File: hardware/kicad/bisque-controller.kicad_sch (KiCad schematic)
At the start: 49 parts, among them J1 USB-C, J2 5V_IN, J3 TC_K, J4 SSR, J5 DISPLAY, J6 NAV_SW, J7 AUX, Q1 AO3400A, Q2 AO3400A, SW1 RESET, SW2 BOOT, U1 ESP32-S3-WROOM-1-N16R8, U2 AMS1117-3.3, U3 MAX31855KASA+, U4 USBLC6-2SC6

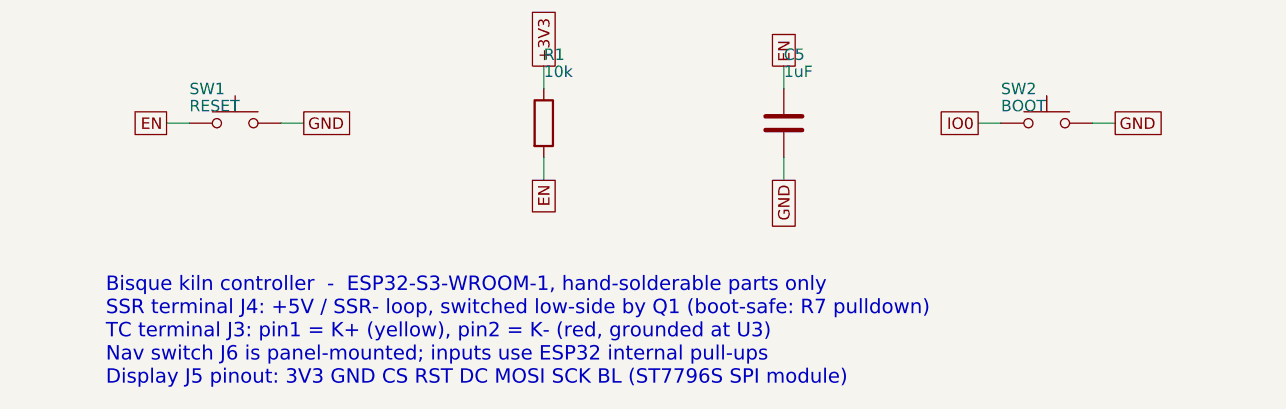
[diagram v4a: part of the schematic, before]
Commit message: hardware: target JLCPCB assembly, fix CPL rotations, refresh fab outputs
Drops the hand-solderable design constraint and makes the board orderable as
an assembled PCBA. Three BOM/CPL defects would have mis-assembled or skipped
parts, and the fab package had drifted from the board file.

gen_jlc.py:
- Apply JLCPCB's per-package rotation corrections when writing the CPL, and
  print each one so a regeneration is auditable. Previously the raw KiCad
  angle went straight through and rotation checking was deferred to JLC's
  order preview, which does not reliably catch 180-degree errors on polarized
  parts. Corrects U2 (SOT-223), Q1/Q2 (SOT-23), U4 (SOT-23-6) and U3
  (SOIC-8). Offsets come from the community table in
  bennymeg/Fabrication-Toolkit, which is derived from real JLCPCB order
  feedback; families absent from it (chip passives, SMA/SOD-123 diodes,
  PLCC-4, USB-C, terminal blocks, 2.54mm headers, tact switches) need no
  correction, so applying a blanket offset to the diodes would have reversed
  D1/D2.
- C9 was LCSC C57112, an imperial 0603 part sitting on an 0805 land pattern.
  Now C1710 (CL21B103KBANNNC, 10nF 50V X7R 0805, Basic).
- BZ1, J5, J6, J7, SW1 and SW2 had blank LCSC numbers, so JLC would not have
  populated them. All six now carry verified in-stock parts. A2547WV-8P was
  rejected for J5/J7 (zero stock) in favour of the genuine Molex 22-27-2081.
- Every entry re-verified against the LCSC catalog for package, value and
  stock; the CONFIRM-at-order-time markers are gone.
- Flag through-hole lines in the BOM (detected from the footprint attr): the
  nine THT parts need JLC's Standard assembly, and its through-hole coverage
  is narrower than its SMD coverage.

Fab outputs: re-exported gerbers, drill, drill map and job file. These were
generated before the board's final zone refill, so F_Cu carried a stale GND
pour outline near the USB-C connector (three vertices collapsing to two,
~80um). Everything else was already geometry-identical. The READM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
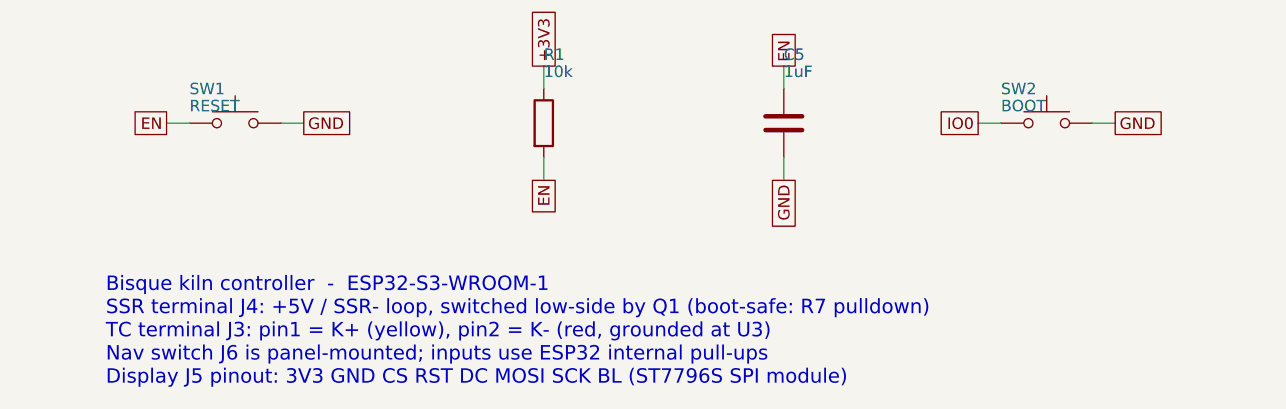
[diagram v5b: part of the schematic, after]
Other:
- note added: "Bisque kiln controller - ESP32-S3-WROOM-1 SSR terminal J4: +5V / SSR- loop, switched low-side by Q1 (boot-safe: R7 pulldown) TC terminal J3: pin1 = K+ (yellow), pin2 = K- (red, grounded at U3) Nav switch J6 is panel-mounted; inputs use ESP32 internal pull-ups Display J5 pinout: 3V3 GND CS RST DC MOSI SCK BL (ST7796S SPI module)"
- note removed: "Bisque kiln controller - ESP32-S3-WROOM-1, hand-solderable parts only SSR terminal J4: +5V / SSR- loop, switched low-side by Q1 (boot-safe: R7 pulldown) TC terminal J3: pin1 = K+ (yellow), pin2 = K- (red, grounded at U3) Nav switch J6 is panel-mounted; inputs use ESP32 internal pull-ups Display J5 pinout: 3V3 GND CS RST DC MOSI SCK BL (ST7796S SPI module)"
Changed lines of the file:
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@@
 		(company "Bisque project")
 		(comment 1 "ESP32-S3-WROOM-1 + MAX31855 + SSR drive")
-		(comment 2 "Hand-solderable: >=0805, SOIC, SOT, THT connectors")
+		(comment 2 "2-layer, 100 x 80 mm, JLCPCB standard process")
 	)
 	(symbol (lib_id "RF_Module:ESP32-S3-WROOM-1") (at 170.18 165.1 0) (unit 1)
@@
 		(effects (font (size 2 2) bold) (justify left))
 	)
-	(text "Bisque kiln controller  -  ESP32-S3-WROOM-1, hand-solderable parts only\nSSR terminal J4: +5V / SSR- loop, switched low-side by Q1 (boot-safe: R7 pulldown)\nTC terminal J3: pin1 = K+ (yellow), pin2 = K- (red, grounded at U3)\nNav switch J6 is panel-mounted; inputs use ESP32 internal pull-ups\nDisplay J5 pinout: 3V3 GND CS RST DC MOSI SCK BL (ST7796S SPI module)" (at 25 281 0)
+	(text "Bisque kiln controller  -  ESP32-S3-WROOM-1\nSSR terminal J4: +5V / SSR- loop, switched low-side by Q1 (boot-safe: R7 pulldown)\nTC terminal J3: pin1 = K+ (yellow), pin2 = K- (red, grounded at U3)\nNav switch J6 is panel-mounted; inputs use ESP32 internal pull-ups\nDisplay J5 pinout: 3V3 GND CS RST DC MOSI SCK BL (ST7796S SPI module)" (at 25 281 0)
 		(effects (font (size 1.6 1.6)) (justify left))
 	)

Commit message: hardware: move display to +5V power, correct 3.5"->4.0" everywhere
Switches the KiCad PCB's display header (J5) from +3V3 to +5V power, per
the user's own hardware: a 4.0" LCDWIKI ST7796S module (MSP4020/MSP4021),
not the 3.5" panel this project previously assumed.

design.py: J5 pin 1 and its local decoupling cap C12 move from +3V3 to
+5V. Verified pin-compatible against the module's own manual (LCDWiki's
product page returned only marketing copy; the linked PDF is a 24-page
scan with no embedded fonts, so it had to be rendered and read directly) -
pins 1-8 are VCC/GND/CS/RESET/DC/SDI/SCK/LED, an exact match for J5's
existing assignment, and VCC is rated 3.3-5V with every reference wiring
diagram in the manual (including 3.3V-logic MCU boards) tying VCC to 5V
while driving the SPI pins directly, no level shifter. No connector or
firmware change needed - same resolution, same driver IC, same GPIOs.

This is the real fix for the AMS1117 (U2) thermal margin flagged in the
prior fab review: the display's backlight and panel logic were the
dominant load the schematic analyzer's power budget never accounted for
(it only sums ICs on a rail). Moving that load to +5V drops U2 back to
just the ESP32 + MAX31855 (~245mA), which keeps its junction temperature
under the datasheet's 125C limit even at a hot enclosure ambient - more
effective than the ground-pour mitigation the prior review proposed.

Rebuilding after the net rename surfaced a real DRC regression: reshaping
+3V3/+5V's routing left one of 197 decorative GND stitching vias isolated
from copper on one layer, a failure mode heal_islands() doesn't cover (it
only bridges pour islands lacking a via, not a via sitting in a clearance
gap). Added drop_disconnected_stitch_vias() to kicad_build.py - safe by
construction, since GND has no point-to-point routing, so every GND via
is decorative and dropping one never touches a real signal connection.
Verified deterministic across rebuilds; DRC is back to 0 errors/0
unconnected a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
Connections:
- net +3V3: no longer C12.1, J5.1 (Pin_1)
- net +5V: now also C12.1, J5.1 (Pin_1)
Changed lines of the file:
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@@
 		(stroke (width 0) (type default))
 	)
-	(global_label "+3V3" (shape passive) (at 31.75 207.01 180)
+	(global_label "+5V" (shape passive) (at 31.75 207.01 180)
 		(effects (font (size 1.27 1.27)) (justify right))
 		(property "Intersheetrefs" "${INTERSHEET_REFS}" (at 31.75 207.01 0)
@@
 		(stroke (width 0) (type default))
 	)
-	(global_label "+3V3" (shape passive) (at 247.65 251.46 90)
+	(global_label "+5V" (shape passive) (at 247.65 251.46 90)
 		(effects (font (size 1.27 1.27)) (justify left))
 		(property "Intersheetrefs" "${INTERSHEET_REFS}" (at 247.65 251.46 0)

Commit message: hardware: cut JLCPCB assembly cost, fix via-in-pad and GND island bugs
Prototype-quantity cost at JLCPCB is dominated by fixed fees, not the BOM
($9.83/board). The board was paying $30 in per-order feeder fees across 10
unique Extended parts, and its 7 through-hole parts forced the Standard
assembly tier ($25 setup) purely to place $1.53/board of connectors.

Cost changes:
- SW1/SW2 swap the 6 mm THT tactile switch for XKB TS-1187A (LCSC C318884),
  a JLCPCB *Basic* part: no feeder fee and it stays on the SMT line.
- The remaining 7 THT parts plus the WS2812B are marked hand-fitted in
  gen_jlc.py and dropped from BOM/CPL, with a new
  jlcpcb/hand-solder-parts.csv shopping list (LCSC + Mouser second source).

Net: 10 unique Extended parts -> 4, $30 -> $12 in feeder fees, and the
order drops from Standard to Economic assembly.

No addressable RGB LED at LCSC is Basic, and substituting discrete R/G/B is
worse (Extended anyway, thin stock, +2 GPIOs, status_led rewrite), so the
5050 is hand-fitted rather than replaced. Likewise no USB-C connector in the
LCSC catalog is Basic or Preferred — max saving from any swap is $0.114/board
against rerouting 9 hand-tuned escape polylines, so C165948 stays.

Bugs found and fixed along the way:
- router.py placed vias inside same-net SMD pads. Clearance rules ignore the
  same-net case and DRC never flags it, but an untented via in a pad wicks
  solder out of the joint during reflow. New VIA_PAD_GAP blocks it; new
  check_via_in_pad.py verifies it against pcbnew geometry (14 conflicts on
  the old board, 0 now).
- kicad_build.py heal_islands() only handled GND islands with no via at all,
  and counted signal vias as anchors. A group of islands that bridged to each
  other but never to the main pour passed the check while KiCad reported a
  missing Zone[GND]/Zone[GND] connection. Rewritten around union-find
  connectivity components.
- check_pcb.py squared circles to their bounding box, over-reporting
  circle-vs-rect distance by up 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
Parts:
- removed C12: 10uF, Capacitor_SMD:C_0805_2012Metric, symbol Device:C
- added C11: 10uF, Capacitor_SMD:C_0805_2012Metric, symbol Device:C
- SW1, SW2: footprint Button_Switch_THT:SW_PUSH_6mm -> Button_Switch_SMD:SW_Push_1P1T_XKB_TS-1187A
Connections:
- net +5V: now also C11.1
- net GND: now also C11.2
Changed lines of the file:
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@@
 			(effects (font (size 1.27 1.27)) (justify left))
 		)
-		(property "Footprint" "Button_Switch_THT:SW_PUSH_6mm" (at 39.37 257.81 0)
+		(property "Footprint" "Button_Switch_SMD:SW_Push_1P1T_XKB_TS-1187A" (at 39.37 257.81 0)
 			(effects (font (size 1.27 1.27)) hide)
 		)
@@
 			(effects (font (size 1.27 1.27)) (justify left))
 		)
-		(property "Footprint" "Button_Switch_THT:SW_PUSH_6mm" (at 129.54 257.81 0)
+		(property "Footprint" "Button_Switch_SMD:SW_Push_1P1T_XKB_TS-1187A" (at 129.54 257.81 0)
 			(effects (font (size 1.27 1.27)) hide)
 		)
@@
 	(symbol (lib_id "Device:C") (at 247.65 257.81 0) (unit 1)
 		(in_bom yes) (on_board yes) (dnp no)
-		(property "Reference" "C12" (at 247.65 250.19 0)
+		(property "Reference" "C11" (at 247.65 250.19 0)
 			(effects (font (size 1.27 1.27)) (justify left))
 		)
@@
 		(pin "1")
 		(pin "2")
-		(instances (project "bisque-controller" (path "/f24e0cd2-71c5-510c-9d15-562ab64c4388" (reference "C12") (unit 1))))
+		(instances (project "bisque-controller" (path "/f24e0cd2-71c5-510c-9d15-562ab64c4388" (reference "C11") (unit 1))))
 	)
 	(wire (pts (xy 247.65 254) (xy 247.65 251.46))
